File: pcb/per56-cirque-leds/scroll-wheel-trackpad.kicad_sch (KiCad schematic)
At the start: 11 parts, among them J2 Conn_01x12_Female, SW1 RotaryEncoder

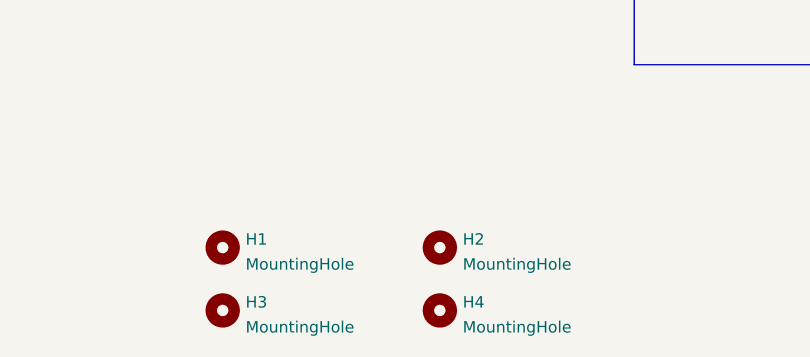
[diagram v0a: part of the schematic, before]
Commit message: added module mounting footprints to make designing both the module pcbs and the keyboard pcbs mounting for modules easier
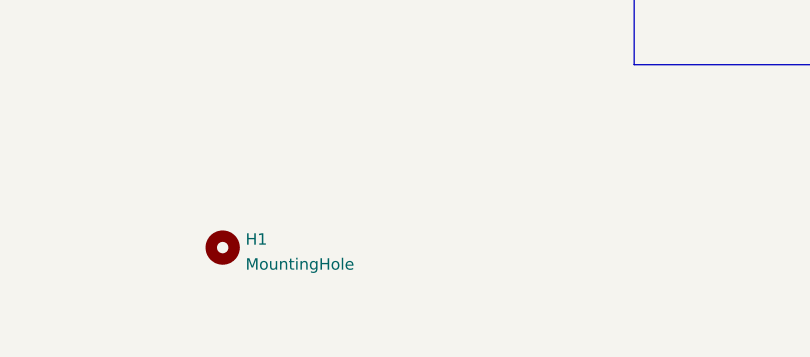
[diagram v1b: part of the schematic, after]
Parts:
- removed H2, H3, H4: MountingHole, MountingHole:MountingHole_2.2mm_M2_Pad, symbol Mechanical:MountingHole
- H1: footprint MountingHole:MountingHole_2.2mm_M2_Pad -> vik:vik-module-mounting-large
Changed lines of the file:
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@@
-    )
-  )
-  (symbol (lib_id "Mechanical:MountingHole") (at 179.07 182.88 0) (unit 1)
-    (in_bom yes) (on_board yes) (dnp no) (fields_autoplaced)
-    (property "Reference" "H2" (at 181.61 181.9715 0)
-      (effects (font (size 1.27 1.27)) (justify left))
-    )
-    (property "Value" "MountingHole" (at 181.61 184.7466 0)
-      (effects (font (size 1.27 1.27)) (justify left))
-    )
-    (property "Footprint" "MountingHole:MountingHole_2.2mm_M2_Pad" (at 179.07 182.88 0)
-      (effects (font (size 1.27 1.27)) hide)
-    )
-    (property "Datasheet" "~" (at 179.07 182.88 0)
-      (effects (font (size 1.27 1.27)) hide)
-    )
-    (instances
-      (project "scroll-wheel-trackpad"
-        (path "/61fe293f-6808-4b7f-9340-9aaac7054a97"
-          (reference "H2") (unit 1)
-        )
-      )
     )
   )
@@
         (path "/61fe293f-6808-4b7f-9340-9aaac7054a97"
           (reference "#PWR0101") (unit 1)
-        )
-      )
-    )
-  )
-  (symbol (lib_id "Mechanical:MountingHole") (at 179.07 189.865 0) (unit 1)
-    (in_bom yes) (on_board yes) (dnp no) (fields_autoplaced)
-    (property "Reference" "H4" (at 181.61 188.9565 0)
-      (effects (font (size 1.27 1.27)) (justify left))
-    )
-    (property "Value" "MountingHole" (at 181.61 191.7316 0)
-      (effects (font (size 1.27 1.27)) (justify left))
-    )
-    (property "Footprint" "MountingHole:MountingHole_2.2mm_M2_Pad" (at 179.07 189.865 0)
-      (effects (font (size 1.27 1.27)) hide)
-    )
-    (property "Datasheet" "~" (at 179.07 189.865 0)
-      (effects (font (size 1.27 1.27)) hide)
-    )
-    (instances
-      (project "scroll-wheel-trackpad"
-        (path "/61fe293f-6808-4b7f-9340-9aaac7054a97"
-          (reference "H4") (unit 1)
         )
       )
@@
       (effects (font (size 1.27 1.27)) (justify left))
     )
-    (property "Footprint" "MountingHole:MountingHole_2.2mm_M2_Pad" (at 154.94 182.88 0)
+    (property "Footprint" "vik:vik-module-mounting-large" (at 154.94 182.88 0)
       (effects (font (size 1.27 1.27)) hide)
     )
@@
         )
       )
-    )
-  )
-  (symbol (lib_id "Mechanical:MountingHole") (at 154.94 189.865 0) (unit 1)
-    (in_bom yes) (on_board yes) (dnp no) (fields_autoplaced)
-    (property "Reference" "H3" (at 157.48 188.9565 0)
-      (effects (font (size 1.27 1.27)) (justify left))
-    )
-    (property "Value" "MountingHole" (at 157.48 191.7316 0)
-      (effects (font (size 1.27 1.27)) (justify left))
-    )
-    (property "Footprint" "MountingHole:MountingHole_2.2mm_M2_Pad" (at 154.94 189.865 0)
-      (effects (font (size 1.27 1.27)) hide)
-    )
-    (property "Datasheet" "~" (at 154.94 189.865 0)
-      (effects (font (size 1.27 1.27)) hide)
-    )
-    (instances
-      (project "scroll-wheel-trackpad"
-        (path "/61fe293f-6808-4b7f-9340-9aaac7054a97"
-          (reference "H3") (unit 1)
-        )
-      )

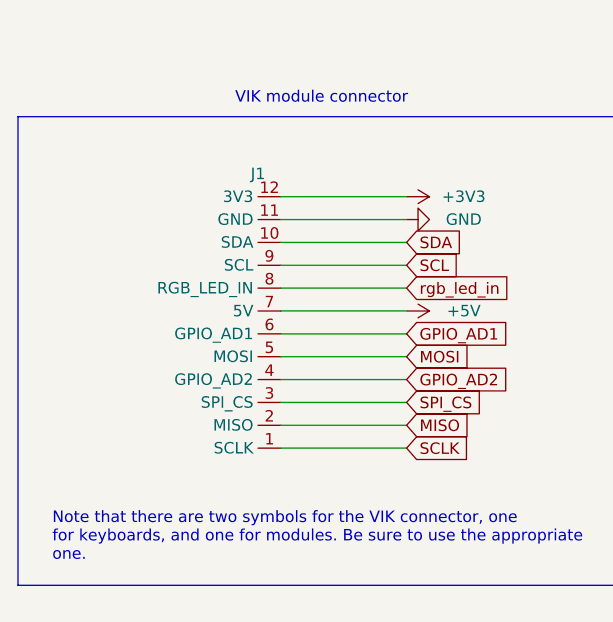
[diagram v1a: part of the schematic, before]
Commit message: updated vikm connector symbols, per some recommendations from sigprof in fingerpunch discord
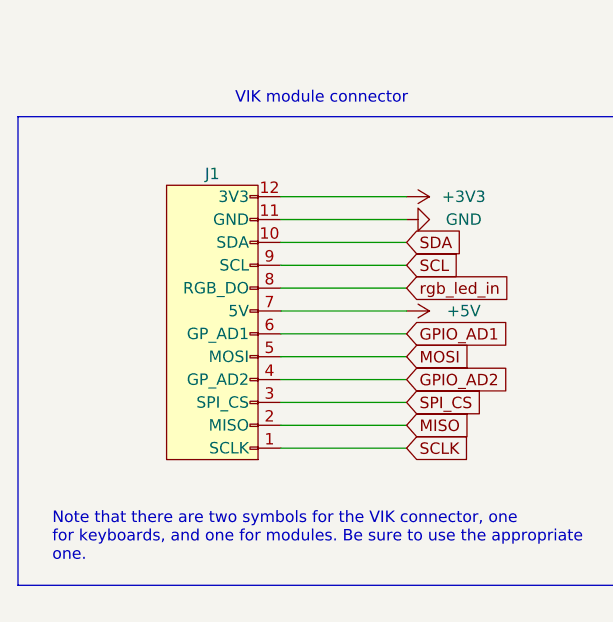
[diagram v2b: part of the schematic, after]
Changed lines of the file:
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@@
     )
   )
-  (symbol (lib_id "vik:vik-module-connector") (at 82.55 72.39 180) (unit 1)
-    (in_bom yes) (on_board yes) (dnp no) (fields_autoplaced)
-    (property "Reference" "J1" (at 80.01 55.88 0)
+  (symbol (lib_id "vik:vik-module-connector") (at 74.93 73.66 180) (unit 1)
+    (in_bom yes) (on_board yes) (dnp no)
+    (property "Reference" "J1" (at 74.93 55.88 0)
       (effects (font (size 1.27 1.27)))
     )
-    (property "Value" "~" (at 82.55 78.74 0)
+    (property "Value" "~" (at 74.93 80.01 0)
       (effects (font (size 1.27 1.27)))
     )
-    (property "Footprint" "vik:vik-module-connector-horizontal" (at 82.55 78.74 0)
+    (property "Footprint" "vik:vik-module-connector-horizontal" (at 74.93 80.01 0)
       (effects (font (size 1.27 1.27)) hide)
     )
-    (property "Datasheet" "" (at 82.55 78.74 0)
+    (property "Datasheet" "" (at 74.93 80.01 0)
       (effects (font (size 1.27 1.27)) hide)
     )
-    (property "LCSC" "C479750" (at 82.55 72.39 0)
+    (property "LCSC" "C479750" (at 74.93 73.66 0)
       (effects (font (size 1.27 1.27)) hide)
     )
